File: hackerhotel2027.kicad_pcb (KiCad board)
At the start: 4 copper layers, 95.4 x 99.9 mm, 358 parts, among them J1 USB device, J2 Battery, Q1 JSM2301S, U1 CH643Q, U2 TPD4E05U06DQAR, U4 XT4054K421MR-G

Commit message: More routing
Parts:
- moved R22 2.00 mm to (-15.8, 9.26)
- moved R2 1.98 mm to (-13.9, 9.24)
- moved R1 1.97 mm to (-14.8, 9.24)
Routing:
- net Net-(D312-A): track 19.9 -> 46.2 mm, vias 0 -> 3
- net R1: track 7.73 -> 9.79 mm
- net R22: track 6.45 -> 5.19 mm
- net R2: track 6.99 -> 8.24 mm
- net /R1b: track 146.7 -> 147.9 mm
- net /R2b: track 159.7 -> 161.0 mm

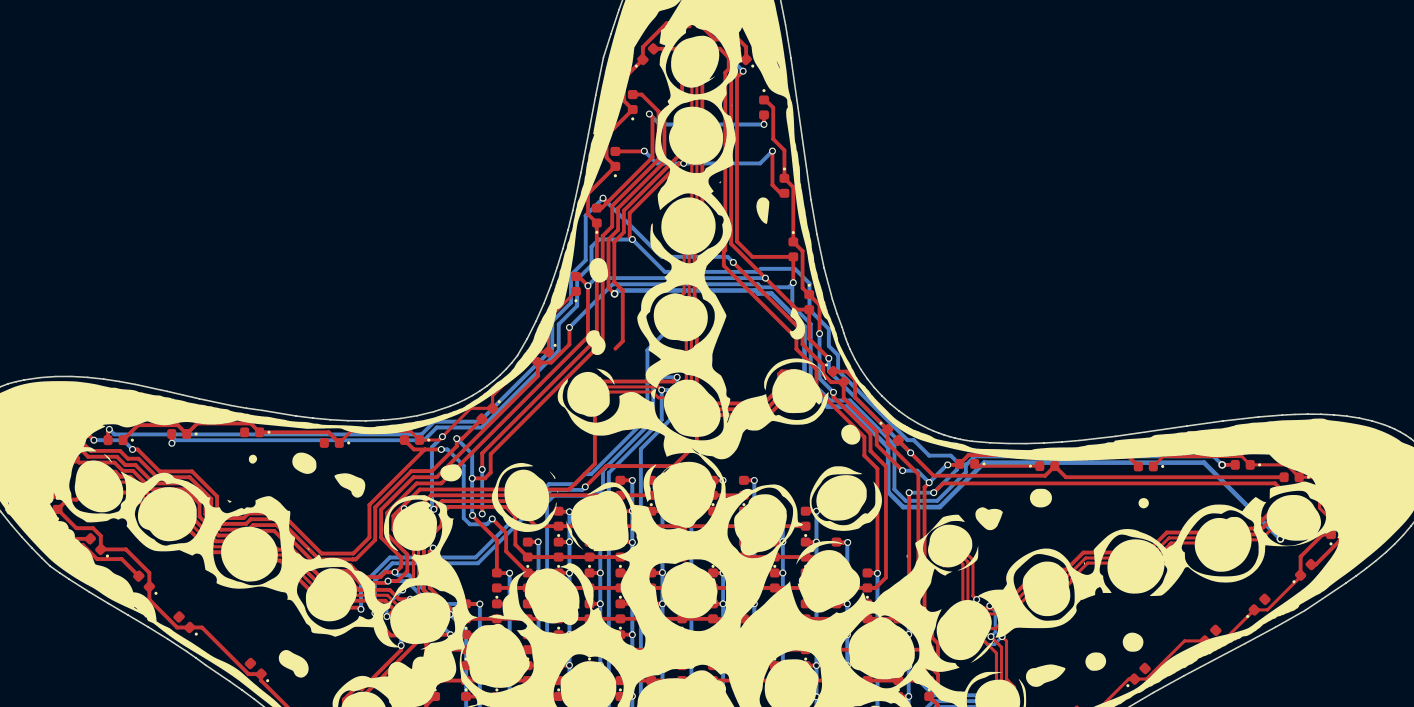
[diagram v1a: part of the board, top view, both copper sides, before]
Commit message: More LED routing
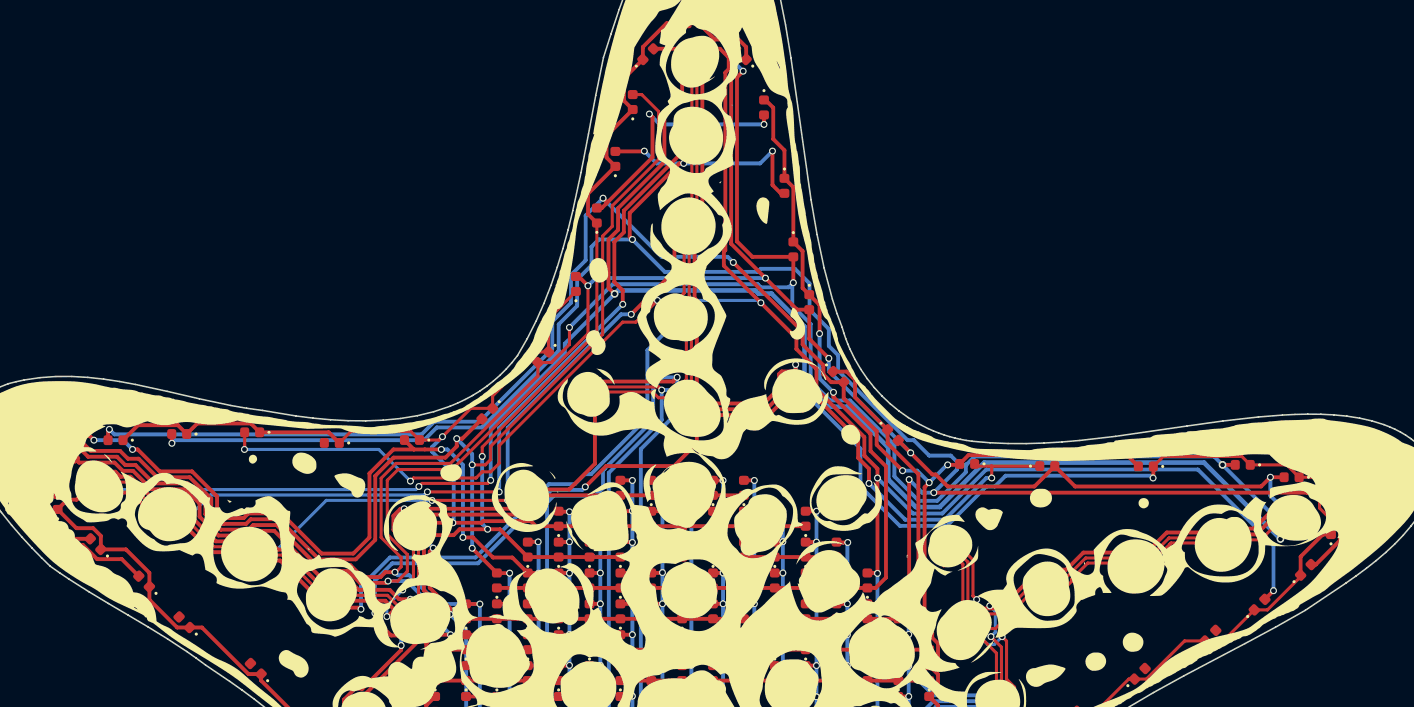
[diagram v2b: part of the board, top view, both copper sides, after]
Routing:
- net Net-(D114-A): track 94.5 -> 169.1 mm, vias 10 -> 16
- net Net-(D308-A): track 73.6 -> 115.1 mm, vias 2 -> 5
- net Net-(D310-A): track 3.36 -> 44.6 mm, vias 2 -> 6
- net Net-(D309-A): track 15.4 -> 50.8 mm, vias 0 -> 4
- net C4: track 116.0 -> 148.3 mm, vias 3 -> 5
- net C5: track 103.6 -> 123.5 mm, vias 3 -> 5
- net /R2b: track 161.0 -> 167.8 mm
- net /R1b: track 147.9 -> 153.9 mm, vias 7 -> 8
- net C13: track 113.3 -> 111.3 mm
- net Net-(D115-A): track 175.1 -> 176.0 mm
